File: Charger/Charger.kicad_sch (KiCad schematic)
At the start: 2 parts, among them J1 Bat_ballanser_conn, J2 Battery_conn

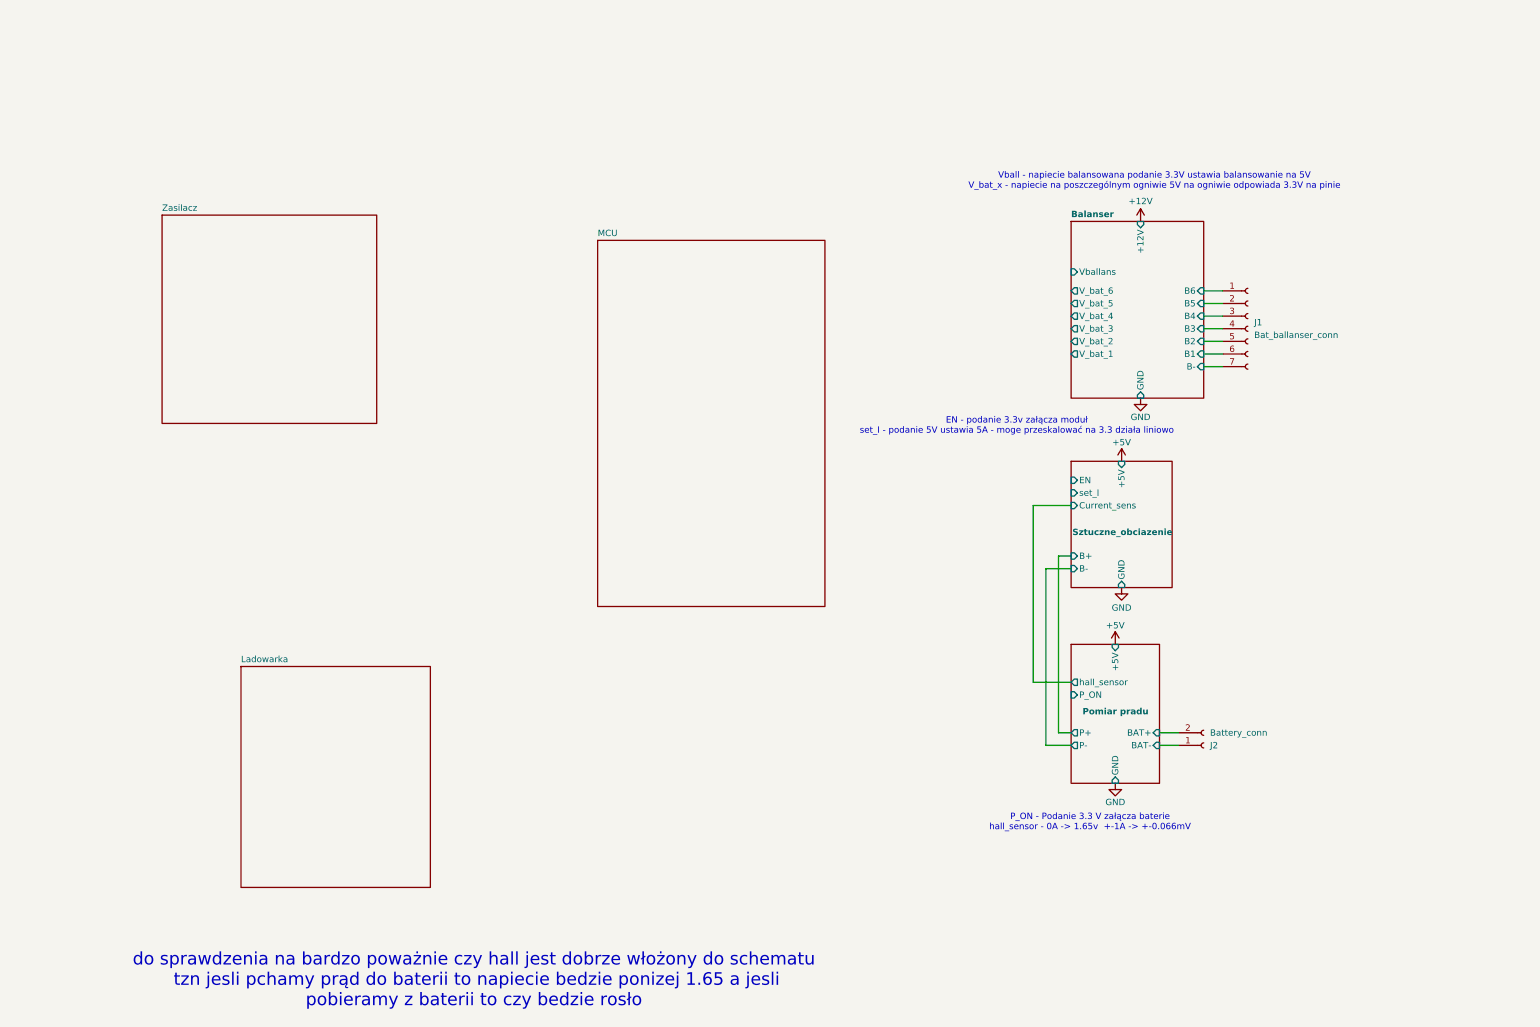
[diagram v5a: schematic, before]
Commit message: dodana ladowarka do glownego projektu
drobne zmiany w sumie wszedzie pozbyłem sie 3.3v poza sterowaniem z pinów mcu, dopiescilem rezystorki zby bylo jak najmniej wartości rozszerzylem delikatnie zakres pradowy przetwornicy
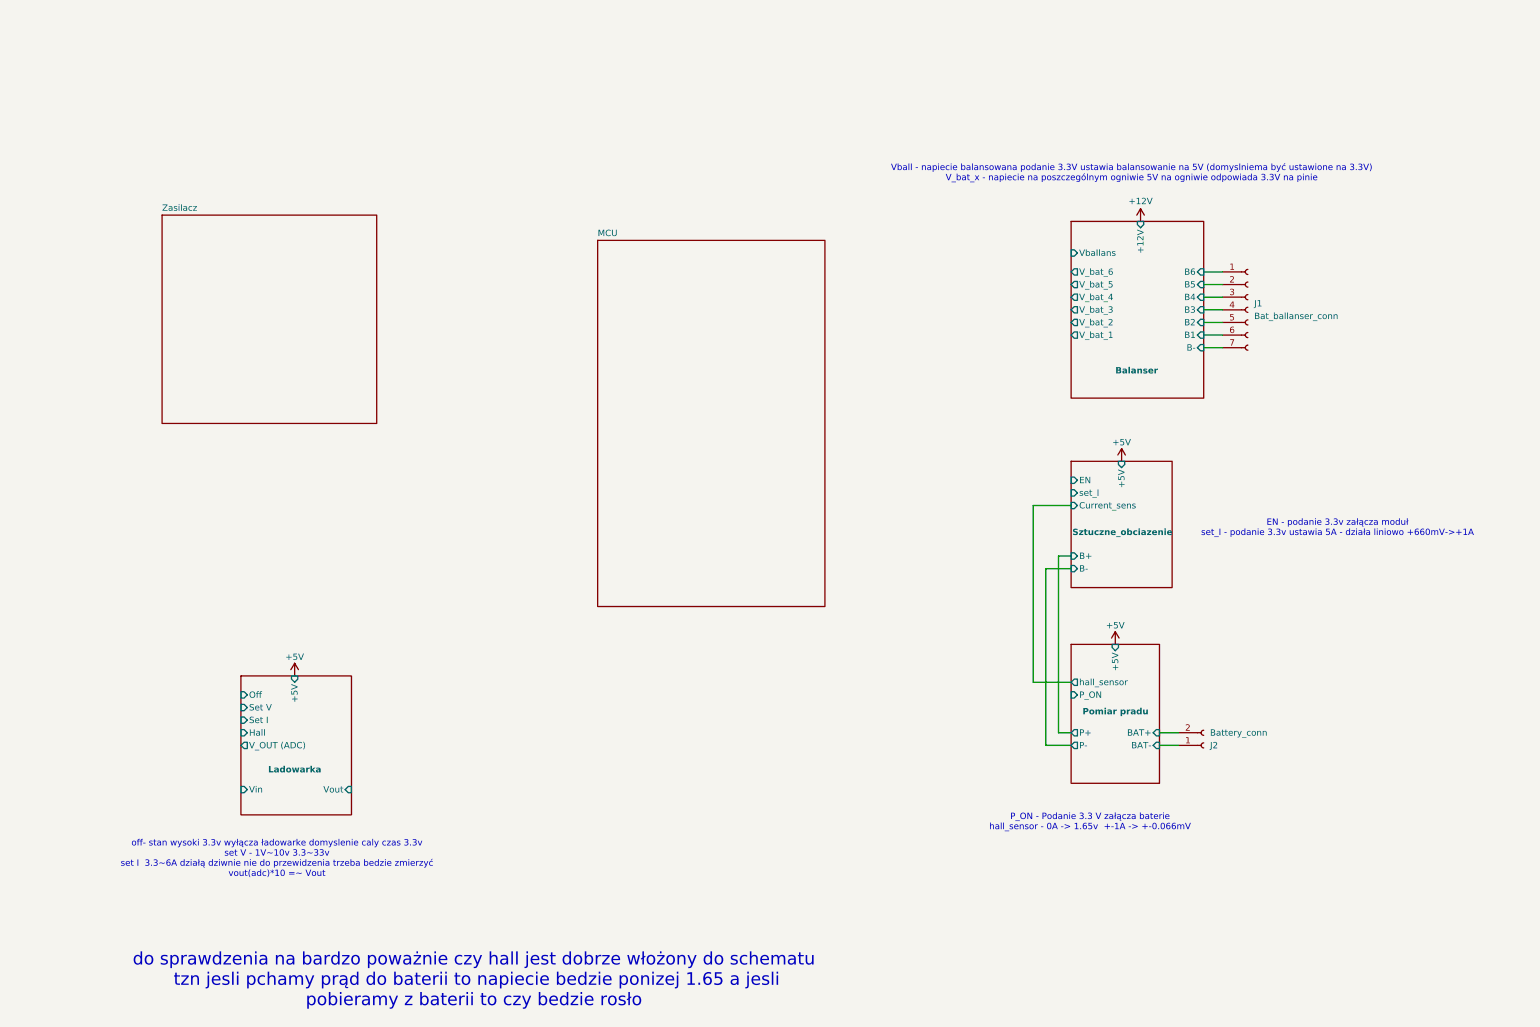
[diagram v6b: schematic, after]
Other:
- sheet Balanser ports: added none; removed GND
- sheet Ladowarka ports: added +5V, Hall, Off, Set I, Set V, V_OUT (ADC), Vin, Vout; removed none
- sheet Pomiar pradu ports: added none; removed GND
- sheet Sztuczne_obciazenie ports: added none; removed GND
- note added: "EN - podanie 3.3v załącza moduł set_I - podanie 3.3v ustawia 5A - działa liniowo +660mV->+1A"
- note added: "Vball - napiecie balansowana podanie 3.3V ustawia balansowanie na 5V (domyslniema być ustawione na 3.3V) V_bat_x - napiecie na poszczególnym ogniwie 5V na ogniwie odpowiada 3.3V na pinie"
- note added: "off- stan wysoki 3.3v wyłącza ładowarke domyslenie caly czas 3.3v set V - 1V~10v 3.3~33v set I 3.3~6A działą dziwnie nie do przewidzenia trzeba bedzie zmierzyć vout(adc)*10 =~ Vout"
- note removed: "EN - podanie 3.3v załącza moduł set_I - podanie 5V ustawia 5A - moge przeskalować na 3.3 działa liniowo"
- note removed: "Vball - napiecie balansowana podanie 3.3V ustawia balansowanie na 5V V_bat_x - napiecie na poszczególnym ogniwie 5V na ogniwie odpowiada 3.3V na pinie"
- moved on the sheet: J1

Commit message: dodanie sekcji zasilacza
i dodanie footprintów prawie wszedzie
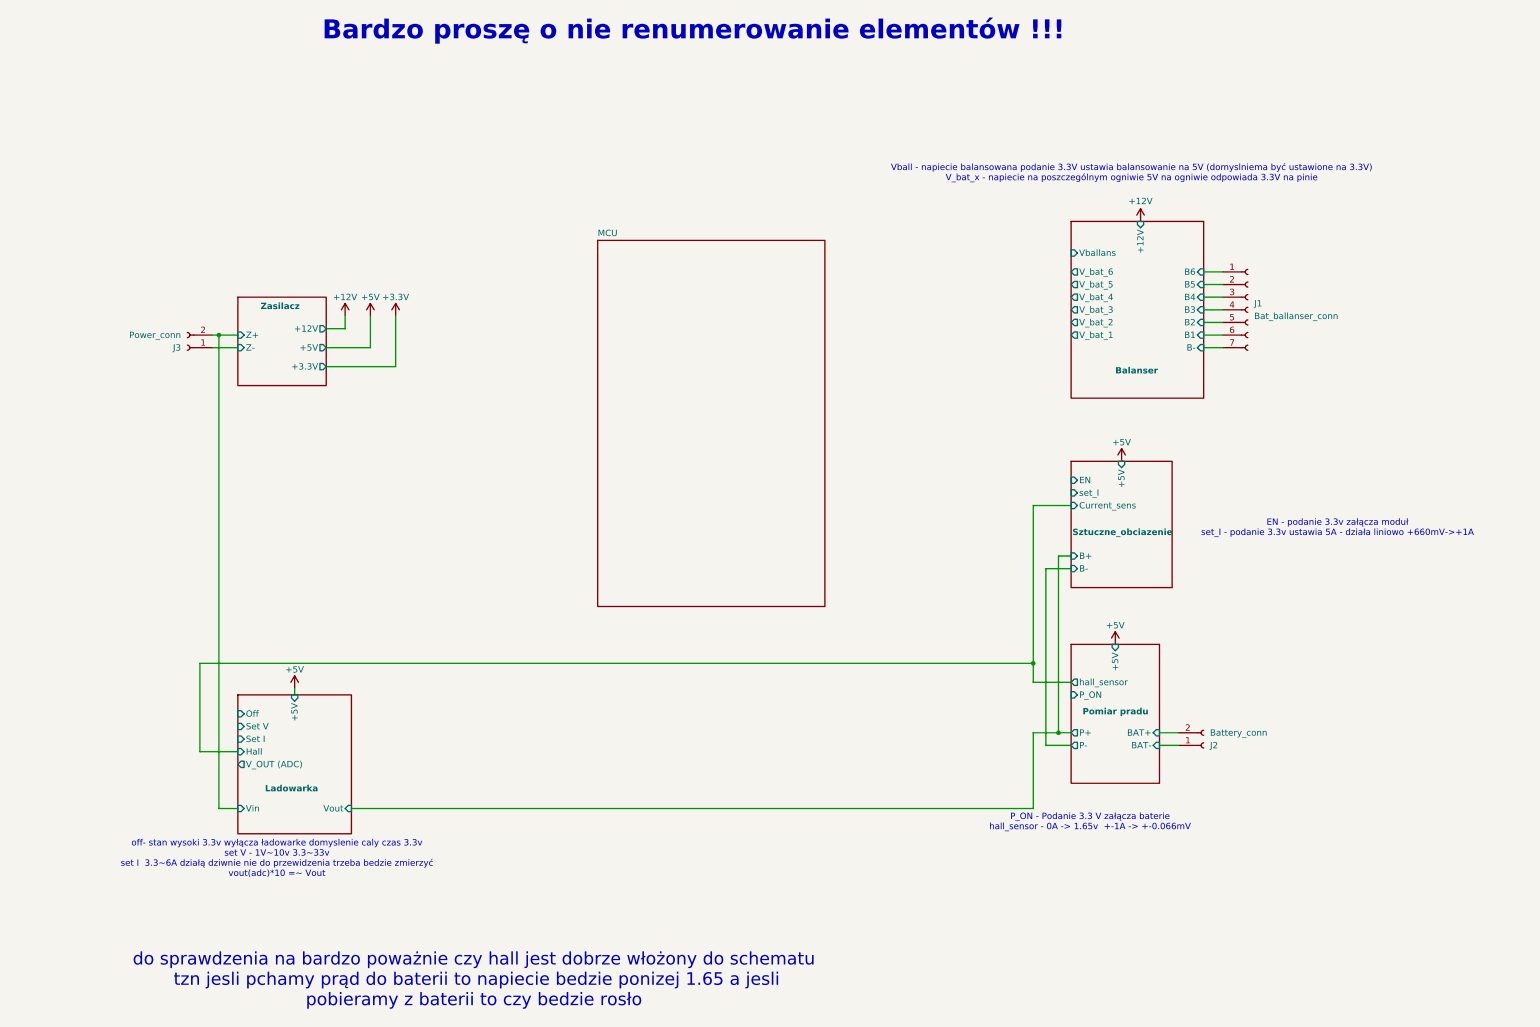
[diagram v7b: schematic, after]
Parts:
- added J3: Power_conn, Connector_AMASS:AMASS_XT60PW-F_1x02_P7.20mm_Horizontal, symbol Connector:Conn_01x02_Socket
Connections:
- net Ladowarka/Vin: now also J3.2 (Pin_2)
- new net Zasilacz/Z-: J3.1 (Pin_1)
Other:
- sheet Zasilacz ports: added +12V, +3.3V, +5V, Z+, Z-; removed none
- note added: "Bardzo proszę o nie renumerowanie elementów !!!"
